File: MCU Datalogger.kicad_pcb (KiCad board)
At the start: 2 copper layers, 49.5 x 26.5 mm, 30 parts, among them J1 Conn_01x04_Pin, J2 Conn_01x04_Pin, J3 Conn_01x09_Pin, J4 Conn_02x03_Odd_Even, U1 24LC1025, U2 24LC1025, U3 DS1337S_, U4 ATMEGA328P-AU, Y1 16 MHz, Y2 32.768kHz

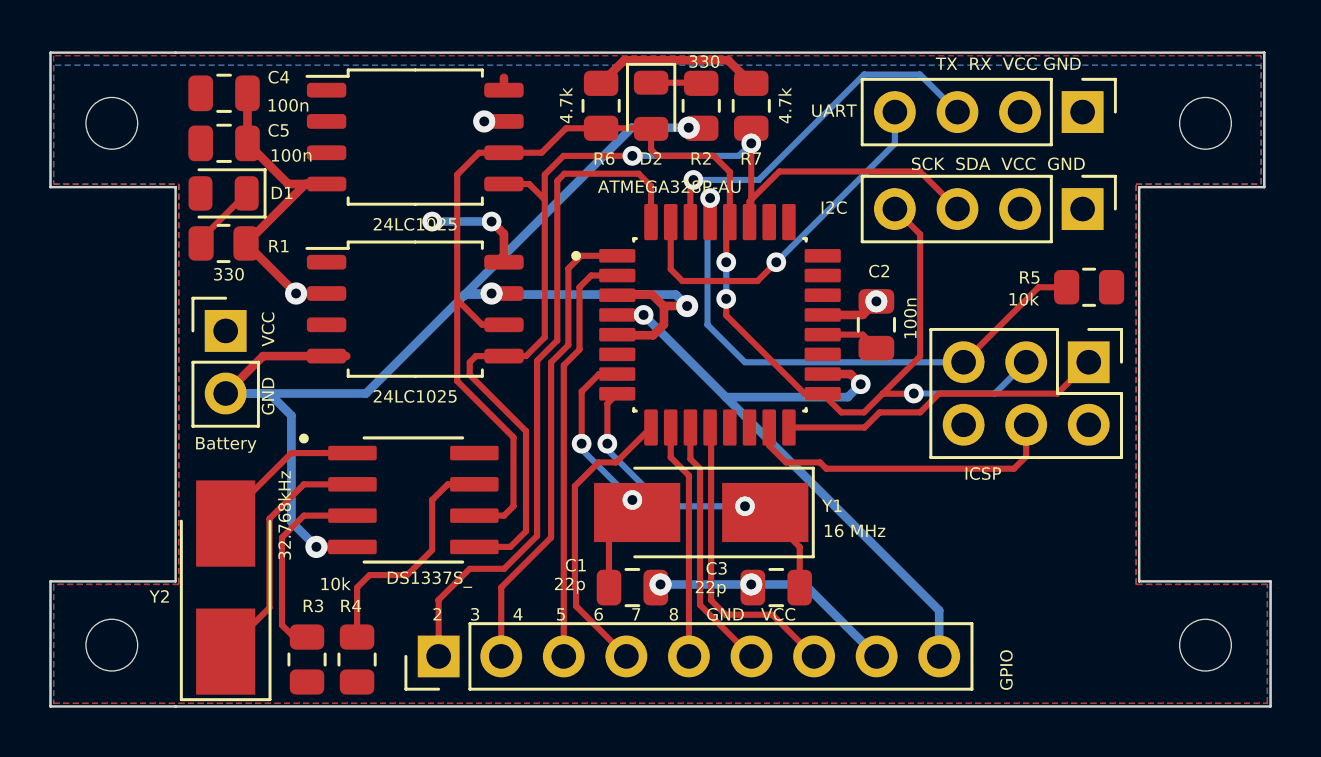
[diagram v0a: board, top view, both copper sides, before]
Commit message: Fixed 2 layer PCB clock issues
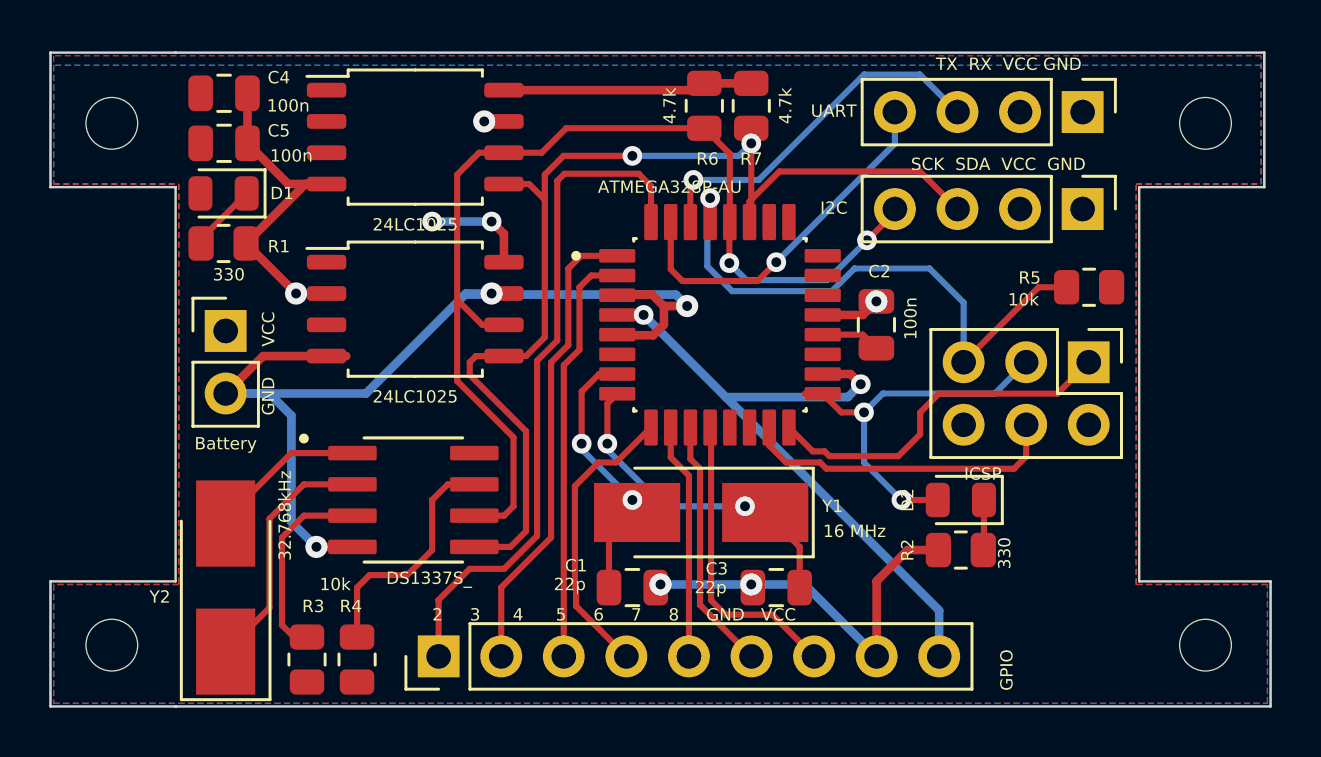
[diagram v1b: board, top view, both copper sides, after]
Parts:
- moved R2 20.9 mm to (160.9, 70.1), turned to 0 degrees
- moved D2 20.4 mm to (160.9, 68.1), turned to 180 degrees
- moved R6 4.19 mm to (150.5, 52.1)
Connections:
- J1 pad 4: /SCK -> /SCL
- R6 pad 2: /SCK -> /SCL
- U1 pad 6: /SCK -> /SCL
- U2 pad 6: /SCK -> /SCL
- U3 pad 6: /SCK -> /SCL
- U4 pad 28: /SCK -> /SCL
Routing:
- net /SCK: track 60.6 -> 15.8 mm, vias 3 -> 2
- net /SCL: track 0.00 -> 43.7 mm, vias 0 -> 2
- net GND: track 83.0 -> 76.5 mm, vias 9 -> 8
- net /Vcc: track 39.5 -> 42.2 mm
- net /MISO: track 13.3 -> 14.8 mm
- net /RESET: track 22.0 -> 22.8 mm
